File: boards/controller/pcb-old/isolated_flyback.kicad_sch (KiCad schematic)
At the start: 20 parts, among them T901 150u

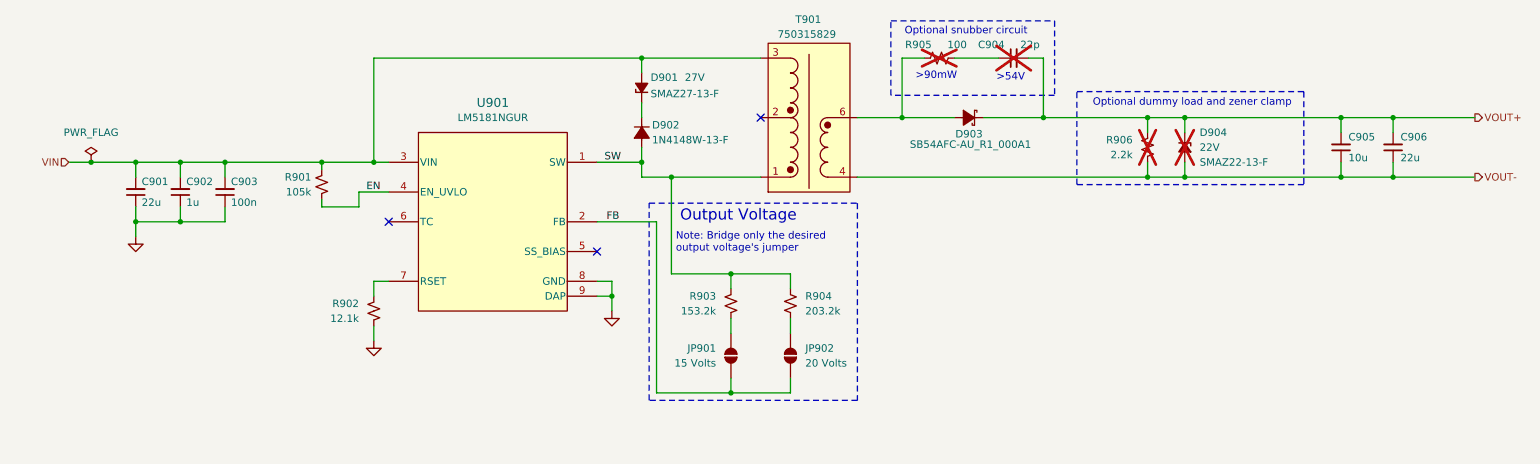
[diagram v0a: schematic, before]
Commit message: controller: pcb: Update schematic
Signed-off-by: Nicholas Loehrke <nicholasnloehrke@gmail.com>
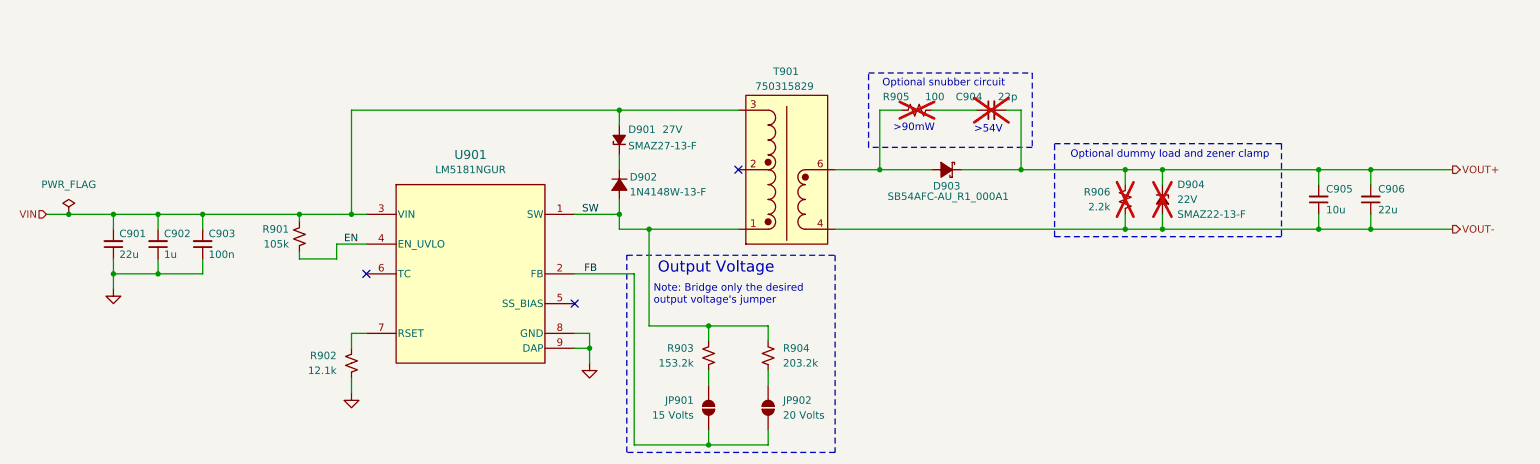
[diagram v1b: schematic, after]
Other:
- moved on the sheet: C901, C902, C903, C904, C905, C906, D901, D902, D903, D904, JP901, JP902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
